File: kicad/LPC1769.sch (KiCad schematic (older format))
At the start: 1 part, among them P1 CONN_LPC1769

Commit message: modificaciones del proyecto Kicad
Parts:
- P1: footprint (none) -> Horno:Pin_Header_LPCXpresso_LPC1769
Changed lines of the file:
@@
 F 0 "P1" H 5400 5100 50  0000 C CNN
 F 1 "CONN_LPC1769" H 5650 2300 50  0000 C CNN
-F 2 "" H 5400 3700 50  0001 C CNN
+F 2 "Horno:Pin_Header_LPCXpresso_LPC1769" H 5400 3700 50  0001 C CNN
 F 3 "" H 5400 3700 50  0000 C CNN
 	1    5850 3700

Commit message: circuito y pcb terminado.
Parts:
- added P8: UART, Pin_Headers:Pin_Header_Straight_1x03, symbol CONN_01X03
- added P9: GPIO, Pin_Headers:Pin_Header_Straight_2x12, symbol CONN_02X12
- added SW1: RST, Buttons_Switches_ThroughHole:SW_PUSH_6mm, symbol SW_PUSH
- P1: value CONN_LPC1769 -> LPC1769
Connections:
- net labels added: +3.3V, +5V, AD_LM35, AD_TERMOCUPLA, GNDA, GNDD, GPIO0, GPIO1, GPIO10, GPIO11, GPIO12, GPIO13, GPIO2, GPIO3, GPIO4, GPIO5, GPIO6, GPIO7, GPIO8, GPIO9, RST, WR
- net labels removed: AD0, AD1, WD
- wire segments 20 -> 75
- no-connect marks 0 -> 12
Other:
- note added: "Comunicación\nUART"
- note added: "Puertos de propósito general\naún sin aplicación."

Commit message: últimas modificaciones al impreso.
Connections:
- net +5V: now also P9.22 (P22); no longer P9.18 (P18), P9.20 (P20)
- net GNDD: no longer P9.21 (P21), P9.22 (P22)
- net GPIO10: now also P1.16 (P0.24/AD0.1); no longer P1.8 (P0.6)
- net GPIO11: now also P1.14 (P0.16); no longer P1.7 (P0.7)
- net GPIO12: now also P1.13 (P0.15); no longer P1.6 (P0.8)
- net GPIO13: now also P1.12 (P0.17); no longer P1.5 (P0.9)
- net GPIO4: now also P1.23 (P0.21); no longer P1.19 (P1.30/AD0.4)
- net GPIO5: now also P1.21 (P0.2/AD0.7); no longer P1.18 (P0.26/AD0.3)
- net GPIO6: now also P1.20 (P1.31/AD0.5); no longer P1.17 (P0.25/AD0.2)
- net GPIO7: now also P1.19 (P1.30/AD0.4); no longer P1.13 (P0.15)
- net GPIO8: now also P1.18 (P0.26/AD0.3); no longer P1.12 (P0.17)
- net GPIO9: now also P1.17 (P0.25/AD0.2); no longer P1.11 (P0.18)
- net GPIO14: now reaches P9.17 (P17)
- net GPIO14: now also P1.11 (P0.18)
- net GPIO16: now reaches P9.19 (P19)
- net GPIO16: now also P1.7 (P0.7)
- new net GPIO15: P1.8 (P0.6), P9.18 (P18)
- new net GPIO17: P1.6 (P0.8), P9.20 (P20)
- new net GPIO18: P1.5 (P0.9), P9.21 (P21)
- no-connect marks 12 -> 5
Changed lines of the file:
@@
 Text Label 4300 4700 0    60   ~ 0
 GPIO3
+Text Label 4300 4600 0    60   ~ 0
+GPIO4
+Text Label 4300 4400 0    60   ~ 0
+GPIO5
+Text Label 4300 4300 0    60   ~ 0
+GPIO6
 Text Label 4300 4200 0    60   ~ 0
-GPIO4
+GPIO7
 Text Label 4300 4100 0    60   ~ 0
-GPIO5
+GPIO8
 Text Label 4300 4000 0    60   ~ 0
-GPIO6
-Text Label 4300 3600 0    60   ~ 0
-GPIO7
-Text Label 4300 3500 0    60   ~ 0
-GPIO8
-Text Label 4300 3400 0    60   ~ 0
 GPIO9
-Text Label 4300 3100 0    60   ~ 0
+Text Label 4300 3900 0    60   ~ 0
 GPIO10
 $Comp
@@
 Wire Wire Line
 	5100 4200 4300 4200
-Text Label 4300 3000 0    60   ~ 0
+Text Label 4300 3700 0    60   ~ 0
 GPIO11
-Text Label 4300 2900 0    60   ~ 0
+Text Label 4300 3600 0    60   ~ 0
 GPIO12
-Text Label 4300 2800 0    60   ~ 0
+Text Label 4300 3500 0    60   ~ 0
 GPIO13
-NoConn ~ 5100 4600
-NoConn ~ 5100 4400
-NoConn ~ 5100 4300
-NoConn ~ 5100 3900
-NoConn ~ 5100 3700
 $Comp
 L GNDD #PWR054
@@
 $EndComp
 Wire Wire Line
-	8300 3400 8300 3050
-Wire Wire Line
-	8300 3050 8550 3050
+	8200 3050 8550 3050
 Wire Wire Line
 	8550 3150 8300 3150
-Connection ~ 8300 3150
 $Comp
 L GNDD #PWR055
@@
 $EndComp
 Wire Wire Line
-	9300 3400 9300 3050
-Wire Wire Line
-	9300 3050 9050 3050
+	9600 3050 9050 3050
 Wire Wire Line
 	9050 3150 9300 3150
-Connection ~ 9300 3150
 $Comp
 L +5V #PWR056
@@
 $EndComp
 Wire Wire Line
-	9600 2750 9600 2950
-Wire Wire Line
-	9600 2950 9050 2950
-Wire Wire Line
-	9050 2850 9600 2850
-Connection ~ 9600 2850
-NoConn ~ 8550 2850
-NoConn ~ 8550 2950
+	9600 2750 9600 3050
+Wire Wire Line
+	5100 3700 4300 3700
+Wire Wire Line
+	5100 3900 4300 3900
+Wire Wire Line
+	5100 4300 4300 4300
+Wire Wire Line
+	5100 4400 4300 4400
+Wire Wire Line
+	5100 4600 4300 4600
+Text Label 4300 3400 0    60   ~ 0
+GPIO14
+Text Label 4300 3100 0    60   ~ 0
+GPIO15
+Text Label 4300 3000 0    60   ~ 0
+GPIO16
+Text Label 4300 2900 0    60   ~ 0
+GPIO17
+Text Label 4300 2800 0    60   ~ 0
+GPIO18
+Wire Wire Line
+	8550 2850 8200 2850
+Wire Wire Line
+	8550 2950 8200 2950
+Wire Wire Line
+	9050 2850 9400 2850
+Text Label 8200 2850 0    60   ~ 0
+GPIO14
+Text Label 9400 2850 2    60   ~ 0
+GPIO15
+Text Label 8200 2950 0    60   ~ 0
+GPIO16
+Text Label 9400 2950 2    60   ~ 0
+GPIO17
+Text Label 8200 3050 0    60   ~ 0
+GPIO18
+Wire Wire Line
+	9050 2950 9400 2950
+Wire Wire Line
+	8300 3150 8300 3400
+Wire Wire Line
+	9300 3150 9300 3400
 $EndSCHEMATC

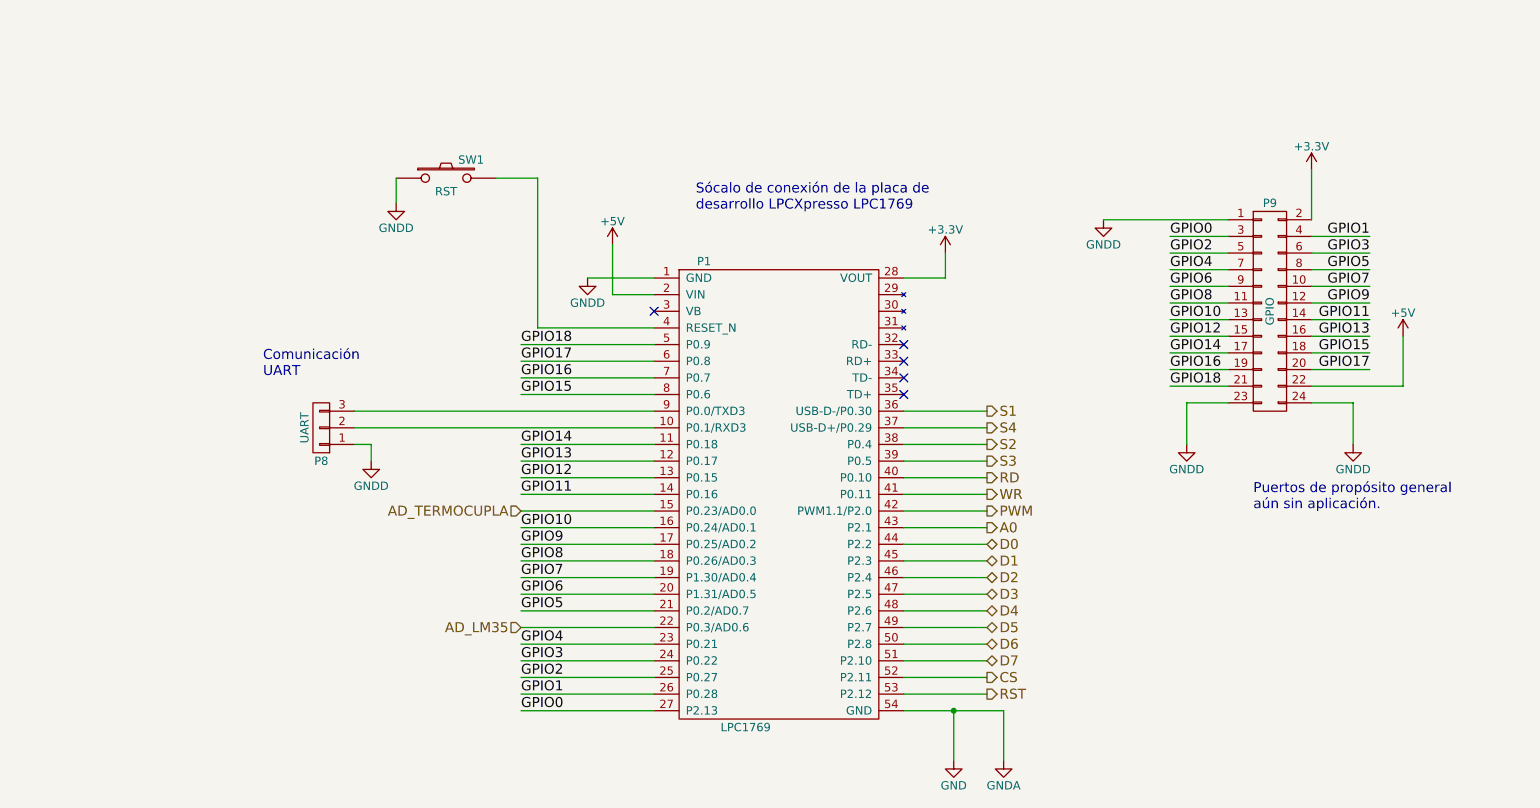
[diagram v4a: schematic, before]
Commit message: Actualizar los esquemáticos
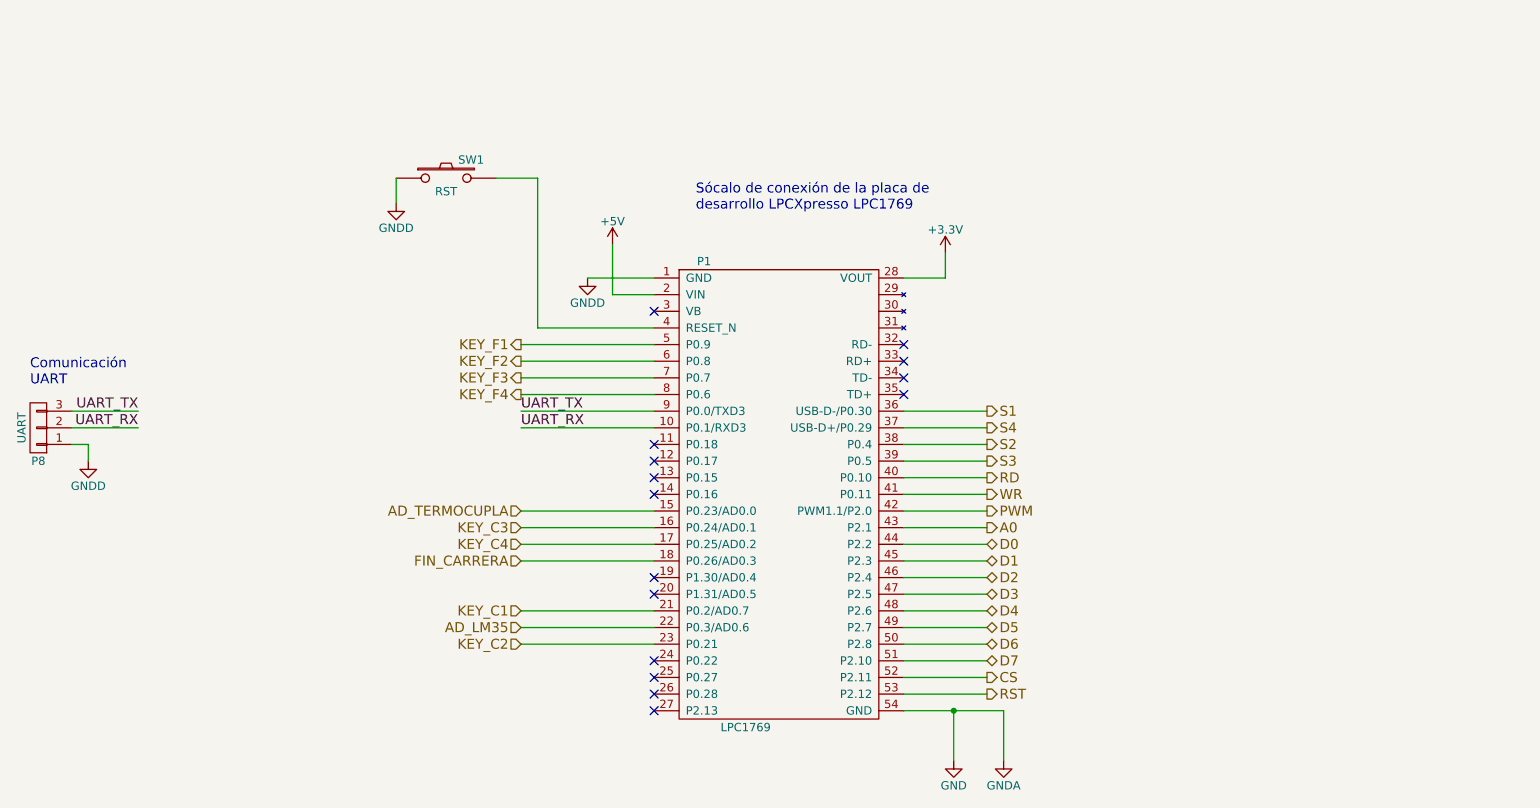
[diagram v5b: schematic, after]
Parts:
- removed P9: GPIO, Pin_Headers:Pin_Header_Straight_2x12, symbol CONN_02X12
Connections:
- net UART_RX: now reaches P1.10 (P0.1/RXD3), P8.2 (P2)
- net UART_TX: now reaches P1.9 (P0.0/TXD3), P8.3 (P3)
- net GPIO0: no longer names the net of P1.27 (P2.13)
- net GPIO1: no longer names the net of P1.26 (P0.28)
- net GPIO10 renamed KEY_C3
- net GPIO11: no longer names the net of P1.14 (P0.16)
- net GPIO12: no longer names the net of P1.13 (P0.15)
- net GPIO13: no longer names the net of P1.12 (P0.17)
- net GPIO14: no longer names the net of P1.11 (P0.18)
- net GPIO15 renamed KEY_F4
- net GPIO16 renamed KEY_F3
- net GPIO17 renamed KEY_F2
- net GPIO18 renamed KEY_F1
- net GPIO2: no longer names the net of P1.25 (P0.27)
- net GPIO3: no longer names the net of P1.24 (P0.22)
- net GPIO4 renamed KEY_C2
- net GPIO5 renamed KEY_C1
- net GPIO6: no longer names the net of P1.20 (P1.31/AD0.5)
- net GPIO7: no longer names the net of P1.19 (P1.30/AD0.4)
- net GPIO8 renamed FIN_CARRERA
- net GPIO9 renamed KEY_C4
- no-connect marks 5 -> 15
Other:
- note removed: "Puertos de propósito general\naún sin aplicación."
- moved on the sheet: P8

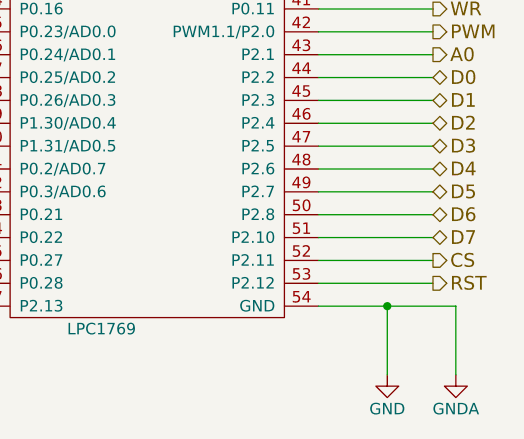
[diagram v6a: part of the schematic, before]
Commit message: Poner la pata de RST del display a 5V
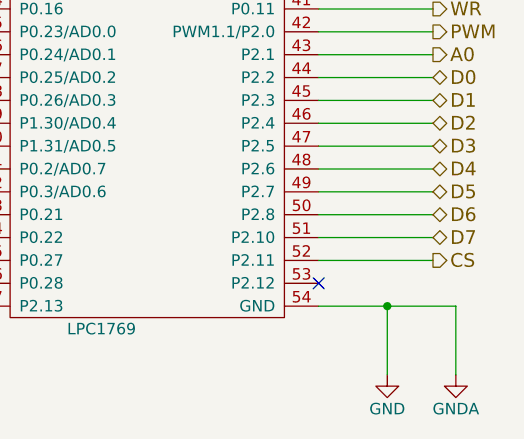
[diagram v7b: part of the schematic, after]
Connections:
- net RST: no longer names the net of P1.53 (P2.12)
- no-connect marks 15 -> 16
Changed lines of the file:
@@
 	1    0    0    -1
 $EndComp
-Text HLabel 7100 4900 2    60   Output ~ 0
-RST
 Text HLabel 4300 3800 0    60   Input ~ 0
 AD_TERMOCUPLA
@@
 Wire Wire Line
 	7100 4800 6600 4800
-Wire Wire Line
-	6600 4900 7100 4900
 Wire Wire Line
 	7100 3700 6600 3700
@@
 Wire Wire Line
 	2000 3300 1600 3300
+NoConn ~ 6600 4900
 $EndSCHEMATC

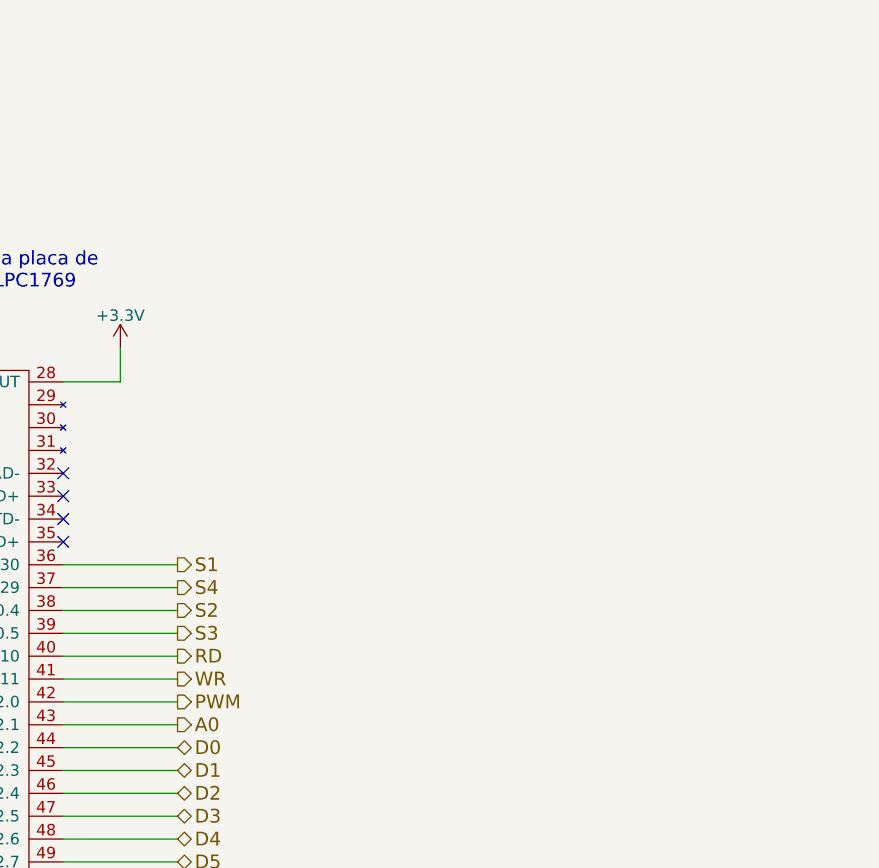
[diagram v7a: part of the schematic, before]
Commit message: agregar LED indicador del PWM.
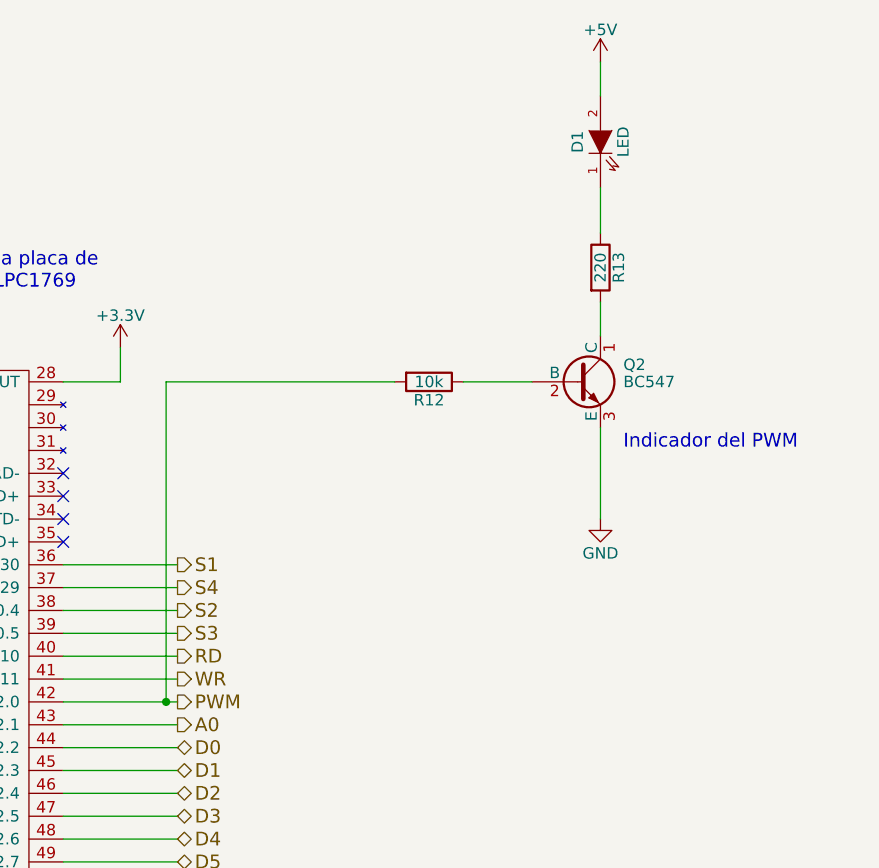
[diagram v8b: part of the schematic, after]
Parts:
- added D1: LED, symbol LED
- added Q2: BC547, TO-92, symbol BC547
- added R12: 10k, symbol R
- added R13: 220, symbol R
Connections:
- net +5V: now also D1.2 (A)
- net GND: now also Q2.3 (E)
- net PWM: now also R12.2
- new net: Q2.1 (C), R13.2
- new net: Q2.2 (B), R12.1
- new net: D1.1 (K), R13.1
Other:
- note added: "Indicador del PWM"
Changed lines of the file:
@@
 Sheet 4 5
 Title "Conexión LPCXpresso LPC1769"
-Date "2016-11-08"
+Date "2016-11-26"
 Rev "3"
 Comp "Elián Hanisch - Rodrigo Oliver - Gastón Riera"
@@
 	2000 3300 1600 3300
 NoConn ~ 6600 4900
+$Comp
+L BC547 Q2
+U 1 1 583A29DB
+P 8850 2400
+F 0 "Q2" H 9050 2475 50  0000 L CNN
+F 1 "BC547" H 9050 2400 50  0000 L CNN
+F 2 "TO-92" H 9050 2325 50  0001 L CIN
+F 3 "" H 8850 2400 50  0000 L CNN
+	1    8850 2400
+	1    0    0    -1
+$EndComp
+$Comp
+L R R13
+U 1 1 583A2A40
+P 8950 1900
+F 0 "R13" V 9030 1900 50  0000 C CNN
+F 1 "220" V 8950 1900 50  0000 C CNN
+F 2 "" V 8880 1900 50  0000 C CNN
+F 3 "" H 8950 1900 50  0000 C CNN
+	1    8950 1900
+	1    0    0    -1
+$EndComp
+$Comp
+L LED D1
+U 1 1 583A2AB1
+P 8950 1350
+F 0 "D1" H 8950 1450 50  0000 C CNN
+F 1 "LED" H 8950 1250 50  0000 C CNN
+F 2 "" H 8950 1350 50  0000 C CNN
+F 3 "" H 8950 1350 50  0000 C CNN
+	1    8950 1350
+	0    -1   -1   0
+$EndComp
+$Comp
+L +5V #PWR53
+U 1 1 583A2AF6
+P 8950 1000
+F 0 "#PWR53" H 8950 850 50  0001 C CNN
+F 1 "+5V" H 8950 1140 50  0000 C CNN
+F 2 "" H 8950 1000 50  0000 C CNN
+F 3 "" H 8950 1000 50  0000 C CNN
+	1    8950 1000
+	1    0    0    -1
+$EndComp
+$Comp
+L R R12
+U 1 1 583A35FD
+P 8200 2400
+F 0 "R12" V 8280 2400 50  0000 C CNN
+F 1 "10k" V 8200 2400 50  0000 C CNN
+F 2 "" V 8130 2400 50  0000 C CNN
+F 3 "" H 8200 2400 50  0000 C CNN
+	1    8200 2400
+	0    1    1    0
+$EndComp
+$Comp
+L GND #PWR54
+U 1 1 583A3630
+P 8950 3000
+F 0 "#PWR54" H 8950 2750 50  0001 C CNN
+F 1 "GND" H 8950 2850 50  0000 C CNN
+F 2 "" H 8950 3000 50  0000 C CNN
+F 3 "" H 8950 3000 50  0000 C CNN
+	1    8950 3000
+	1    0    0    -1
+$EndComp
+Wire Wire Line
+	8950 3000 8950 2600
+Wire Wire Line
+	8950 2200 8950 2050
+Wire Wire Line
+	8950 1750 8950 1550
+Wire Wire Line
+	8950 1000 8950 1150
+Wire Wire Line
+	8650 2400 8350 2400
+Wire Wire Line
+	8050 2400 7050 2400
+Wire Wire Line
+	7050 2400 7050 3800
+Connection ~ 7050 3800
+Text Notes 9050 2700 0    60   ~ 0
+Indicador del PWM
 $EndSCHEMATC
